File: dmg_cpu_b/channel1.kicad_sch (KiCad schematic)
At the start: 123 parts

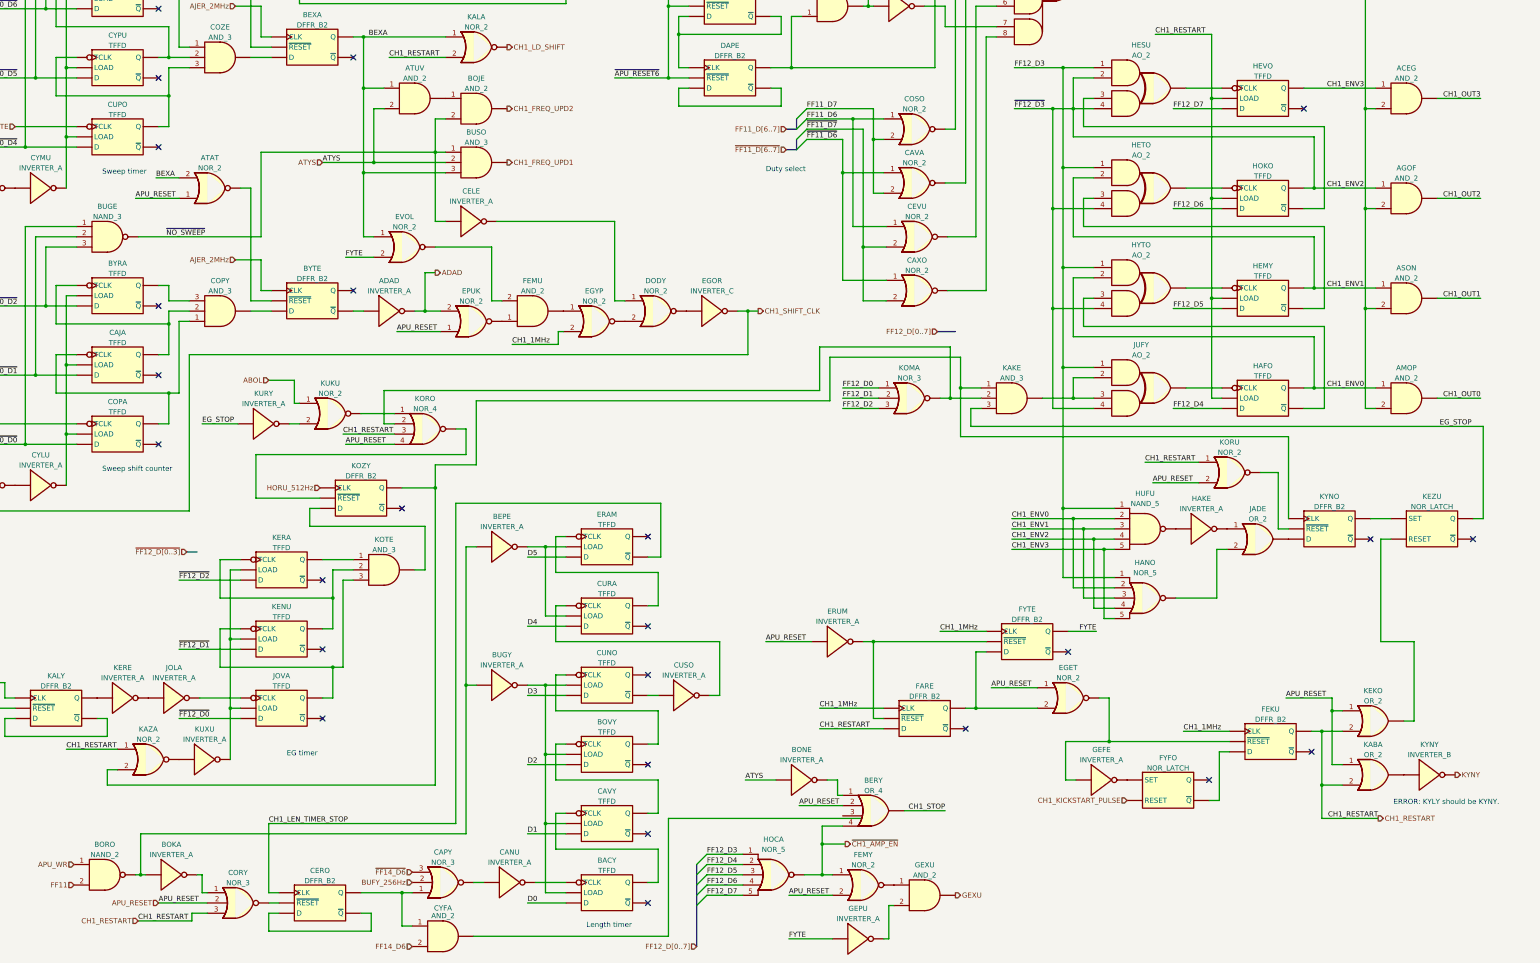
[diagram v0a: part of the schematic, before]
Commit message: Channel 2 + Channel 3 added. Channel 3 fits on 2 sheets.
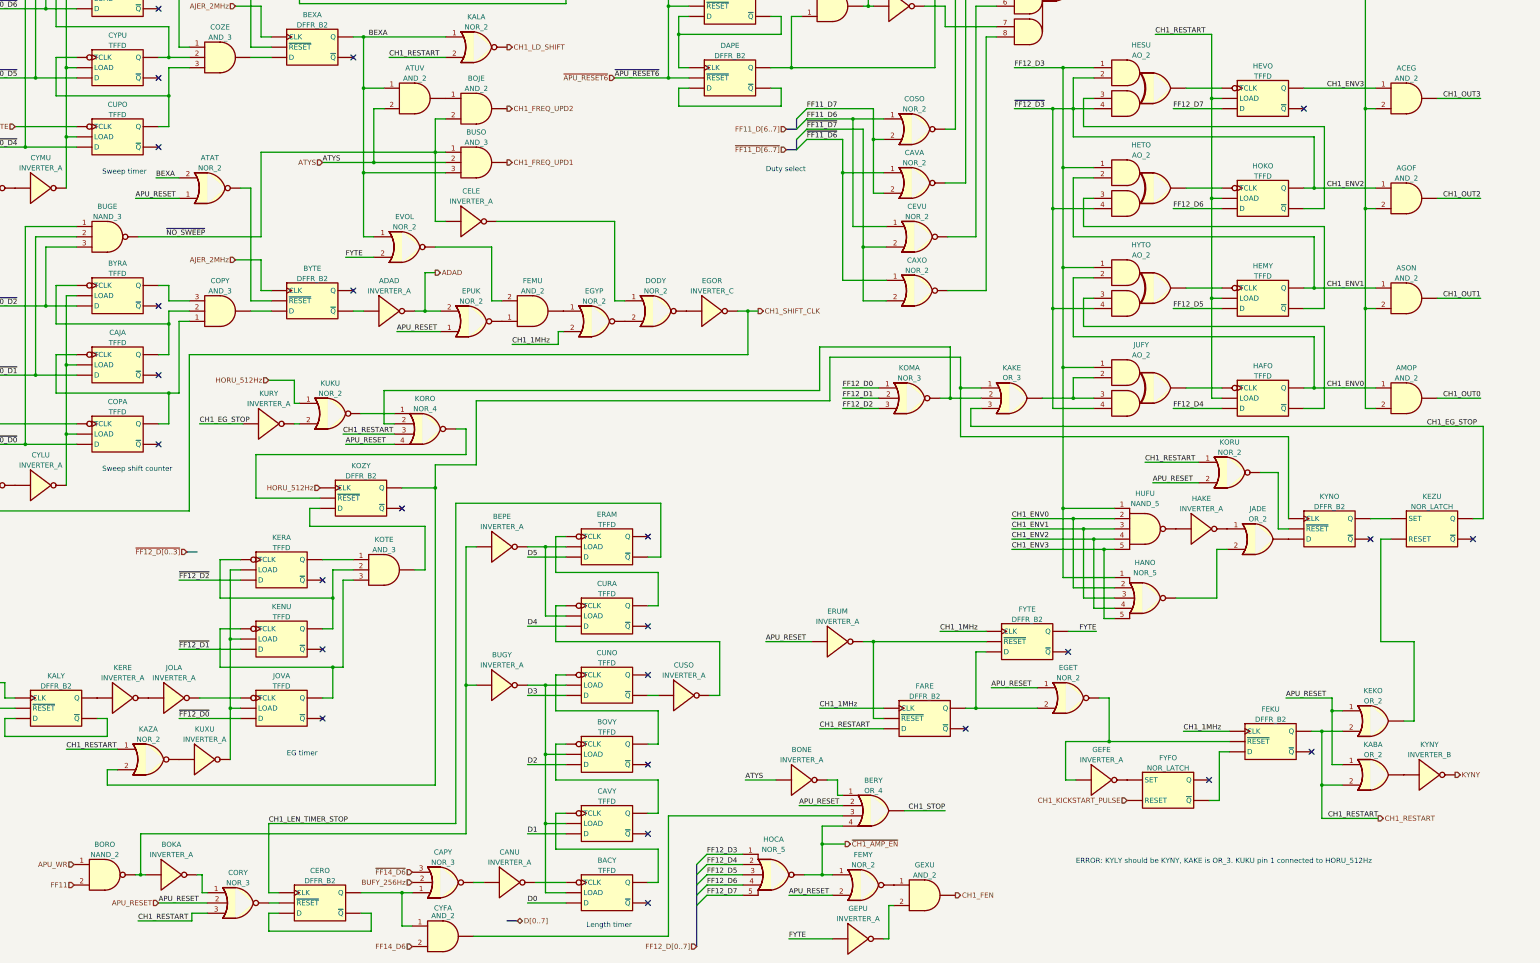
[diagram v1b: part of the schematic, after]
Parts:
- KAKE: value AND_3 -> OR_3; symbol DMG_CPU_Cells:AND_3 -> DMG_CPU_Cells:OR_3
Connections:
- net ABOL is gone; now on net HORU_512Hz: KUKU.1
- net at BERY.3: now also CYFA.3
- net EG_STOP renamed CH1_EG_STOP
- net GEXU renamed CH1_FEN
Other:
- note added: "ERROR: KYLY should be KYNY, KAKE is OR_3. KUKU pin 1 connected to HORU_512Hz"
- note removed: "ERROR: KYLY should be KYNY."
- moved on the sheet: KURY
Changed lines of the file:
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@@
     (stroke (width 0) (type default) (color 0 0 0 0))
   )
+  (bus (pts (xy 165.1 274.955) (xy 167.64 274.955))
+    (stroke (width 0) (type default) (color 0 0 0 0))
+  )
   (wire (pts (xy 156.845 33.02) (xy 156.845 37.465))
     (stroke (width 0) (type default) (color 0 0 0 0))
@@
     (stroke (width 0) (type default) (color 0 0 0 0))
   )
-  (wire (pts (xy 111.125 151.765) (xy 113.665 151.765))
+  (wire (pts (xy 112.395 151.765) (xy 113.665 151.765))
     (stroke (width 0) (type default) (color 0 0 0 0))
   )
@@
     (stroke (width 0) (type default) (color 0 0 0 0))
   )
-  (wire (pts (xy 89.535 151.765) (xy 98.425 151.765))
+  (wire (pts (xy 88.9 151.765) (xy 99.695 151.765))
     (stroke (width 0) (type default) (color 0 0 0 0))
   )
@@
     (stroke (width 0) (type default) (color 0 0 0 0))
   )
-  (wire (pts (xy 205.105 249.555) (xy 205.105 278.765))
+  (wire (pts (xy 205.105 248.92) (xy 205.105 278.765))
     (stroke (width 0) (type default) (color 0 0 0 0))
   )
@@
     (stroke (width 0) (type default) (color 0 0 0 0))
   )
-  (bus (pts (xy 271.78 128.905) (xy 276.225 128.905))
-    (stroke (width 0) (type default) (color 0 0 0 0))
-  )
   (wire (pts (xy 124.46 190.5) (xy 124.46 212.09))
     (stroke (width 0) (type default) (color 0 0 0 0))
@@
     (stroke (width 0) (type default) (color 0 0 0 0))
   )
-  (wire (pts (xy 205.105 249.555) (xy 252.73 249.555))
+  (wire (pts (xy 205.105 248.92) (xy 248.285 248.92))
     (stroke (width 0) (type default) (color 0 0 0 0))
   )
@@
     (stroke (width 0) (type default) (color 0 0 0 0))
   )
-  (text "ERROR: KYLY should be KYNY." (at 384.81 246.38 0)
+  (text "ERROR: KYLY should be KYNY, KAKE is OR_3. KUKU pin 1 connected to HORU_512Hz"
+    (at 306.07 260.985 0)
     (effects (font (size 1.27 1.27)) (justify left bottom))
   )
@@
     (effects (font (size 1.27 1.27)) (justify left bottom))
   )
-  (label "EG_STOP" (at 89.535 151.765 0)
+  (label "CH1_EG_STOP" (at 88.9 151.765 0)
     (effects (font (size 1.27 1.27)) (justify left bottom))
   )
@@
     (effects (font (size 1.27 1.27)) (justify left bottom))
   )
-  (label "EG_STOP" (at 396.24 152.4 0)
+  (label "CH1_EG_STOP" (at 393.065 152.4 0)
     (effects (font (size 1.27 1.27)) (justify left bottom))
   )
@@
     (effects (font (size 1.27 1.27)) (justify left))
   )
-  (hierarchical_label "GEXU" (shape output) (at 276.225 268.605 0)
+  (hierarchical_label "CH1_FEN" (shape output) (at 276.225 268.605 0)
     (effects (font (size 1.27 1.27)) (justify left))
   )
-  (hierarchical_label "FF12_D[0..7]" (shape input) (at 271.78 128.905 180)
-    (effects (font (size 1.27 1.27)) (justify right))
-  )
-  (hierarchical_label "CH1_RESTART" (shape input) (at 73.66 274.955 180)
-    (effects (font (size 1.27 1.27)) (justify right))
-  )
   (hierarchical_label "APU_WR" (shape input) (at 57.785 260.985 180)
     (effects (font (size 1.27 1.27)) (justify right))
   )
-  (hierarchical_label "ABOL" (shape input) (at 106.045 140.97 180)
+  (hierarchical_label "HORU_512Hz" (shape input) (at 106.045 140.97 180)
     (effects (font (size 1.27 1.27)) (justify right))
   )
+  (hierarchical_label "D[0..7]" (shape bidirectional) (at 167.64 274.955 0)
+    (effects (font (size 1.27 1.27)) (justify left))
+  )
   (hierarchical_label "FF11_D[6..7]" (shape input) (at 234.315 78.74 180)
     (effects (font (size 1.27 1.27)) (justify right))
@@
     (effects (font (size 1.27 1.27)) (justify right))
   )
+  (hierarchical_label "~{APU_RESET6}" (shape input) (at 191.77 66.04 180)
+    (effects (font (size 1.27 1.27)) (justify right))
+  )
   (hierarchical_label "~{FF12_D[0..3]}" (shape input) (at 85.725 183.515 180)
     (effects (font (size 1.27 1.27)) (justify right))
@@
     (pin "4")
   )
-  (symbol (lib_id "DMG_CPU_Cells:INVERTER_A") (at 104.775 151.765 0) (unit 1)
+  (symbol (lib_id "DMG_CPU_Cells:INVERTER_A") (at 106.045 151.765 0) (unit 1)
     (in_bom yes) (on_board yes) (fields_autoplaced)
-    (property "Reference" "KURY" (id 0) (at 104.775 144.2552 0))
-    (property "Value" "INVERTER_A" (id 1) (at 104.775 146.7921 0))
-    (property "Footprint" "" (id 2) (at 102.235 151.765 0)
+    (property "Reference" "KURY" (id 0) (at 106.045 144.2552 0))
+    (property "Value" "INVERTER_A" (id 1) (at 106.045 146.7921 0))
+    (property "Footprint" "" (id 2) (at 103.505 151.765 0)
       (effects (font (size 1.27 1.27)) hide)
     )
-    (property "Datasheet" "http://iceboy.a-singer.de/doc/dmg_cells.html#inv_a" (id 3) (at 106.045 159.385 0)
+    (property "Datasheet" "http://iceboy.a-singer.de/doc/dmg_cells.html#inv_a" (id 3) (at 107.315 159.385 0)
       (effects (font (size 1.27 1.27)) hide)
     )
@@
     (pin "2")
   )
-  (symbol (lib_id "DMG_CPU_Cells:AND_3") (at 290.195 145.415 0) (unit 1)
-    (in_bom yes) (on_board yes) (fields_autoplaced)
+  (symbol (lib_id "DMG_CPU_Cells:OR_3") (at 290.195 145.415 0) (unit 1)
+    (in_bom yes) (on_board yes)
     (property "Reference" "KAKE" (id 0) (at 290.195 137.9052 0))
-    (property "Value" "AND_3" (id 1) (at 290.195 140.4421 0))
-    (property "Footprint" "" (id 2) (at 290.195 145.415 0)
+    (property "Value" "OR_3" (id 1) (at 290.195 140.335 0))
+    (property "Footprint" "" (id 2) (at 289.941 145.415 0)
       (effects (font (size 1.27 1.27)) hide)
     )
-    (property "Datasheet" "http://iceboy.a-singer.de/doc/dmg_cells.html#and3" (id 3) (at 290.195 153.035 0)
+    (property "Datasheet" "http://iceboy.a-singer.de/doc/dmg_cells.html#or3" (id 3) (at 290.195 153.035 0)
       (effects (font (size 1.27 1.27)) hide)
     )

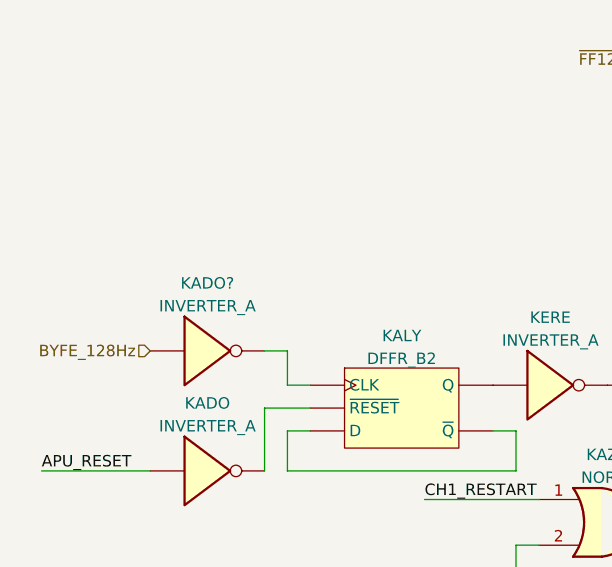
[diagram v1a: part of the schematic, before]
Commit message: fixes made following review
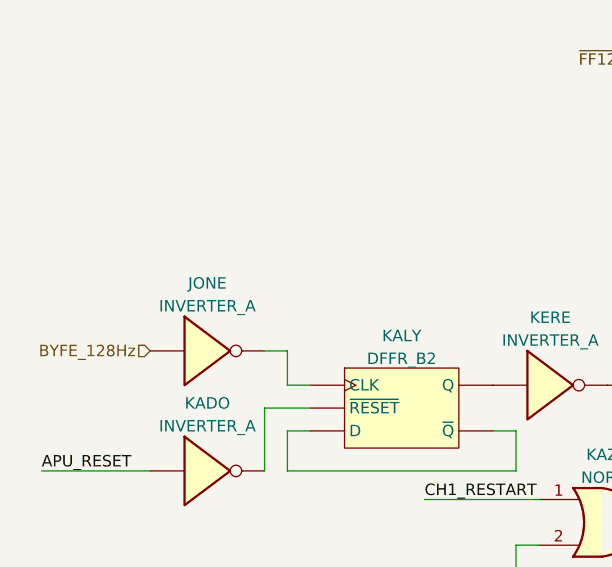
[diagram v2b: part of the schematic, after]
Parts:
- gave numbers to parts that had none: 1
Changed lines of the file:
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@@
   (symbol (lib_id "DMG_CPU_Cells:INVERTER_A") (at 31.75 215.9 0) (unit 1)
     (in_bom yes) (on_board yes) (fields_autoplaced)
-    (property "Reference" "KADO?" (id 0) (at 31.75 208.3902 0))
+    (property "Reference" "JONE" (id 0) (at 31.75 208.3902 0))
     (property "Value" "INVERTER_A" (id 1) (at 31.75 210.9271 0))
     (property "Footprint" "" (id 2) (at 29.21 215.9 0)

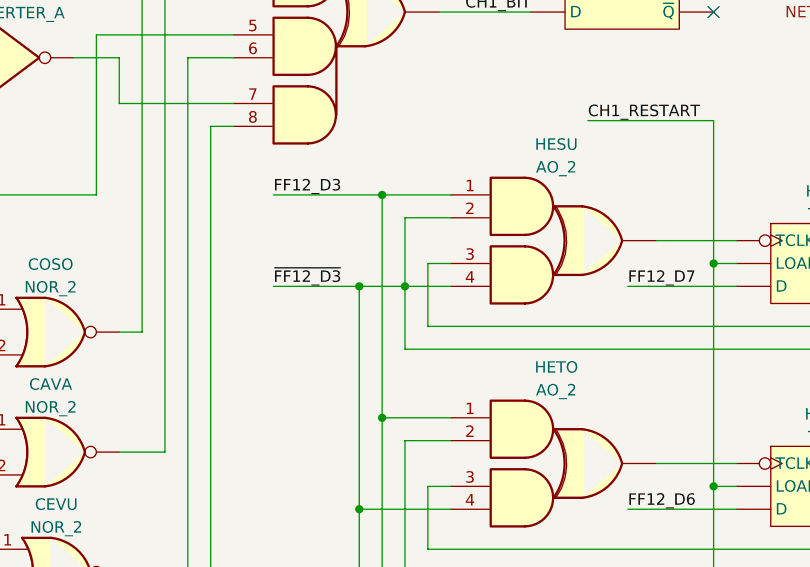
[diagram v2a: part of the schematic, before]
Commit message: Fixes made from issues, channel 4 sheet aded and tidy up of hierarchical APU sheet. Small fixes done here and there when doing ERC.
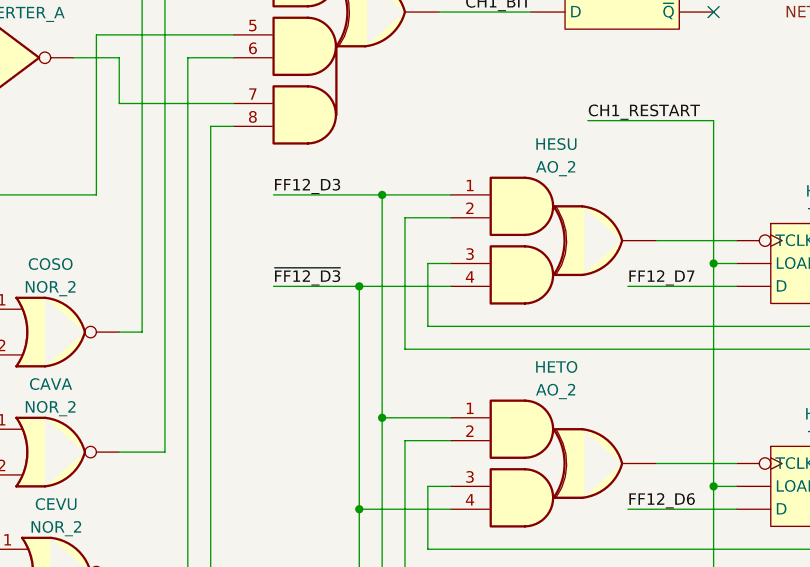
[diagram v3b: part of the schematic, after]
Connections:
- net CH1_ENV2: no longer HESU.4, HETO.4, HYTO.4, JUFY.4
- new net ~{FF12_D3}: HESU.4, HETO.4, HYTO.4, JUFY.4
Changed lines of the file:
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@@
   (junction (at 205.105 66.04) (diameter 0) (color 0 0 0 0)
   )
+  (junction (at 300.355 73.66) (diameter 0) (color 0 0 0 0)
+  )
   (junction (at 342.265 22.225) (diameter 0) (color 0 0 0 0)
   )
@@
   (junction (at 174.625 216.535) (diameter 0) (color 0 0 0 0)
   )
-  (junction (at 300.355 73.66) (diameter 0) (color 0 0 0 0)
-  )
   (junction (at 81.28 70.485) (diameter 0) (color 0 0 0 0)
   )
@@
   )
   (junction (at 367.03 227.965) (diameter 0) (color 0 0 0 0)
-  )
-  (junction (at 305.435 73.66) (diameter 0) (color 0 0 0 0)
   )
   (junction (at 274.955 145.415) (diameter 0) (color 0 0 0 0)
@@
     (stroke (width 0) (type default) (color 0 0 0 0))
   )
-  (wire (pts (xy 300.355 73.66) (xy 305.435 73.66))
-    (stroke (width 0) (type default) (color 0 0 0 0))
-  )
   (wire (pts (xy 129.54 68.58) (xy 134.62 68.58))
     (stroke (width 0) (type default) (color 0 0 0 0))
@@
     (stroke (width 0) (type default) (color 0 0 0 0))
   )
-  (wire (pts (xy 305.435 73.66) (xy 310.515 73.66))
-    (stroke (width 0) (type default) (color 0 0 0 0))
-  )
   (wire (pts (xy 83.82 224.79) (xy 99.06 224.79))
     (stroke (width 0) (type default) (color 0 0 0 0))
@@
     (stroke (width 0) (type default) (color 0 0 0 0))
   )
+  (wire (pts (xy 300.355 73.66) (xy 310.515 73.66))
+    (stroke (width 0) (type default) (color 0 0 0 0))
+  )
   (wire (pts (xy 106.045 273.05) (xy 106.045 277.495))
     (stroke (width 0) (type default) (color 0 0 0 0))
@@
     (stroke (width 0) (type default) (color 0 0 0 0))
   )
-  (wire (pts (xy 305.435 73.66) (xy 305.435 80.645))
+  (wire (pts (xy 305.435 66.04) (xy 305.435 80.645))
     (stroke (width 0) (type default) (color 0 0 0 0))
   )
@@
     (stroke (width 0) (type default) (color 0 0 0 0))
   )
-  (wire (pts (xy 305.435 66.04) (xy 305.435 73.66))
-    (stroke (width 0) (type default) (color 0 0 0 0))
-  )

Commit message: Fixes made based on raised issues. PPU decode page added as draft level.
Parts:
- DAPE, EROS: value DFFR_B2 -> DFFR_B; symbol DMG_CPU_Cells:DFFR_B2 -> DMG_CPU_Cells:DFFR_B
- GEXU: value AND_2 -> NAND_LATCH; symbol DMG_CPU_Cells:AND_2 -> DMG_CPU_Cells:NAND_LATCH
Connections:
- net CH1_EG_STOP: no longer KURY.1
- net ~{APU_RESET6}: now also DAPE.1 (~{RESET}), DAPE.5 (~{RESET}), EROS.1 (~{RESET}), EROS.5 (~{RESET}); no longer DAPE.2 (~{RESET}), DAPE.4 (~{RESET}), EROS.2 (~{RESET}), EROS.4 (~{RESET})
- net at GEXU.2 (~{Q}): no longer GEPU.2
- net at DUNA.5, EZOZ.1: now also DAPE.7 (Q); no longer DAPE.6 (Q)
- net at HAKE.2: now also JADE.2; no longer JADE.1
- net at KAKE.1, KAZA.2, KOZY.6 (Q)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: now also KURY.1
- net at ESUT.3 (D), ESUT.5 (~{Q}): now also EROS.3 (CLK), EROS.4 (~{CLK}); no longer EROS.1 (CLK)
- net at EZOZ.2: now also EROS.7 (Q); no longer EROS.6 (Q)
- net at HANO.6: now also JADE.1; no longer JADE.2
- net at DAPE.3 (CLK): now also DAPE.4 (~{CLK}), EROS.2 (D), EROS.6 (~{Q}); no longer DAPE.5 (~{Q})
- new net: GEPU.2, GEXU.4 (~{SET})
- new net: DAPE.2 (D), DAPE.6 (~{Q})
- no-connect marks 27 -> 28
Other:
- note added: "EG timer clocked at 64Hz"
- note removed: "EG timer"
- moved on the sheet: BERY, BONE, EGET, ERUM, FARE, FEKU, FEMY, FYFO, FYTE, GEFE, GEPU, HOCA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

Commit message: Further fixes made based on raised issues.
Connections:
- net CH1_EG_STOP: now also KEZU.2 (~{Q}); no longer KEZU.3 (Q)
- net CH1_FDIS: now reaches GEXU.2 (~{Q})
- net CH1_FEN: no longer names the net of GEXU.3 (Q)
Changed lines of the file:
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@@
   (no_connect (at 127 60.96))
   (no_connect (at 200.025 201.93))
+  (no_connect (at 404.495 175.26))
   (no_connect (at 78.74 139.7))
   (no_connect (at 119.38 201.93))
@@
   (no_connect (at 200.025 253.365))
   (no_connect (at 200.025 270.51))
-  (no_connect (at 346.075 242.57))
+  (no_connect (at 346.075 237.49))
   (no_connect (at 339.725 43.18))
   (no_connect (at 119.38 184.785))
   (no_connect (at 259.715 227.33))
   (no_connect (at 200.025 213.995))
-  (no_connect (at 404.495 180.34))
   (no_connect (at 172.72 160.02))
   (no_connect (at 379.095 180.34))
@@
     (stroke (width 0) (type default) (color 0 0 0 0))
   )
-  (wire (pts (xy 407.035 175.26) (xy 407.035 152.4))
+  (wire (pts (xy 407.035 152.4) (xy 407.035 180.34))
     (stroke (width 0) (type default) (color 0 0 0 0))
   )
@@
     (stroke (width 0) (type default) (color 0 0 0 0))
   )
-  (wire (pts (xy 404.495 175.26) (xy 407.035 175.26))
+  (wire (pts (xy 404.495 180.34) (xy 407.035 180.34))
     (stroke (width 0) (type default) (color 0 0 0 0))
   )
@@
     (stroke (width 0) (type default) (color 0 0 0 0))
   )
-  (wire (pts (xy 347.345 237.49) (xy 346.075 237.49))
+  (wire (pts (xy 348.615 242.57) (xy 346.075 242.57))
     (stroke (width 0) (type default) (color 0 0 0 0))
   )
@@
     (effects (font (size 1.27 1.27)) (justify left))
   )
-  (hierarchical_label "CH1_FEN" (shape output) (at 347.345 237.49 0)
+  (hierarchical_label "CH1_FDIS" (shape output) (at 348.615 242.57 0)
     (effects (font (size 1.27 1.27)) (justify left))
   )

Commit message: Fixes made based on raised issues (in APU sheets).
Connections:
- net CH1_EG_STOP: now also KEZU.3 (Q); no longer KEZU.2 (~{Q})
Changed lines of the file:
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@@
   (no_connect (at 127 60.96))
   (no_connect (at 200.025 201.93))
-  (no_connect (at 404.495 175.26))
+  (no_connect (at 404.495 180.34))
   (no_connect (at 78.74 139.7))
   (no_connect (at 119.38 201.93))
@@
     (stroke (width 0) (type default) (color 0 0 0 0))
   )
-  (wire (pts (xy 407.035 152.4) (xy 407.035 180.34))
+  (wire (pts (xy 407.035 152.4) (xy 407.035 175.26))
     (stroke (width 0) (type default) (color 0 0 0 0))
   )
@@
     (stroke (width 0) (type default) (color 0 0 0 0))
   )
-  (wire (pts (xy 404.495 180.34) (xy 407.035 180.34))
-    (stroke (width 0) (type default) (color 0 0 0 0))
-  )
+  (wire (pts (xy 404.495 175.26) (xy 407.035 175.26))
+    (stroke (width 0) (type default) (color 0 0 0 0))
+  )
